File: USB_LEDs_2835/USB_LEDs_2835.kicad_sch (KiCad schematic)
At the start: 53 parts, among them U1 MT9284, U2 JL8022W-L, U3 74LVC1G04

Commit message: Add files via upload
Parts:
- added JP1: solderjumper_1, Jumper:SolderJumper-3_P1.3mm_Bridged12_Pad1.0x1.5mm_NumberLabels, symbol Jumper:SolderJumper_3_Bridged12
- added JP2: solderjumper_2, Jumper:SolderJumper-3_P1.3mm_Bridged12_Pad1.0x1.5mm_NumberLabels, symbol Jumper:SolderJumper_3_Bridged12
- Cx1: value 1u -> 22u; footprint Capacitor_SMD:C_0402_1005Metric -> Capacitor_SMD:C_0603_1608Metric
- D1, D10, D11, D12, D13, D14, D15, D16, D17, D18, D19, D2, D20, D21, D22, D23, D24, D25, D26, D27, D28, D29, D3, D30, D31, D32, D4, D5, D6, D7, D8, D9: footprint LED_SMD:LED_2835 -> LED_SMD:LED_2835_custom_margin
- R1: footprint Resistor_SMD:R_0402_1005Metric -> Resistor_SMD:R_0603_1608Metric
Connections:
- net +5V: now also JP1.1 (A), JP2.3 (B); no longer U2.6 (OPT1)
- net GND: now also JP1.3 (B), JP2.1 (A); no longer U2.8 (OPT2)
- new net: JP1.2 (C), U2.6 (OPT1)
- new net: JP2.2 (C), U2.8 (OPT2)
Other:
- moved on the sheet: C2, H1, H2

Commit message: Add files via upload
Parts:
- D33: footprint Diode_SMD:D_SOD-323 -> Diode_SMD:D_SOD-323_custom
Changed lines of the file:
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@@
       (effects (font (size 1.27 1.27)) (justify left))
     )
-    (property "Footprint" "Diode_SMD:D_SOD-323" (id 2) (at 98.298 78.105 0)
+    (property "Footprint" "Diode_SMD:D_SOD-323_custom" (id 2) (at 98.298 78.105 0)
       (effects (font (size 1.27 1.27)) hide)
     )
@@
     )
     (path "/a4553eb6-c1f2-4b4d-a632-f4d917a8f586"
-      (reference "D33") (unit 1) (value "1N4148WS") (footprint "Diode_SMD:D_SOD-323")
+      (reference "D33") (unit 1) (value "1N4148WS") (footprint "Diode_SMD:D_SOD-323_custom")
     )
     (path "/076783c6-7e48-4539-88e9-ef3e20bf1349"

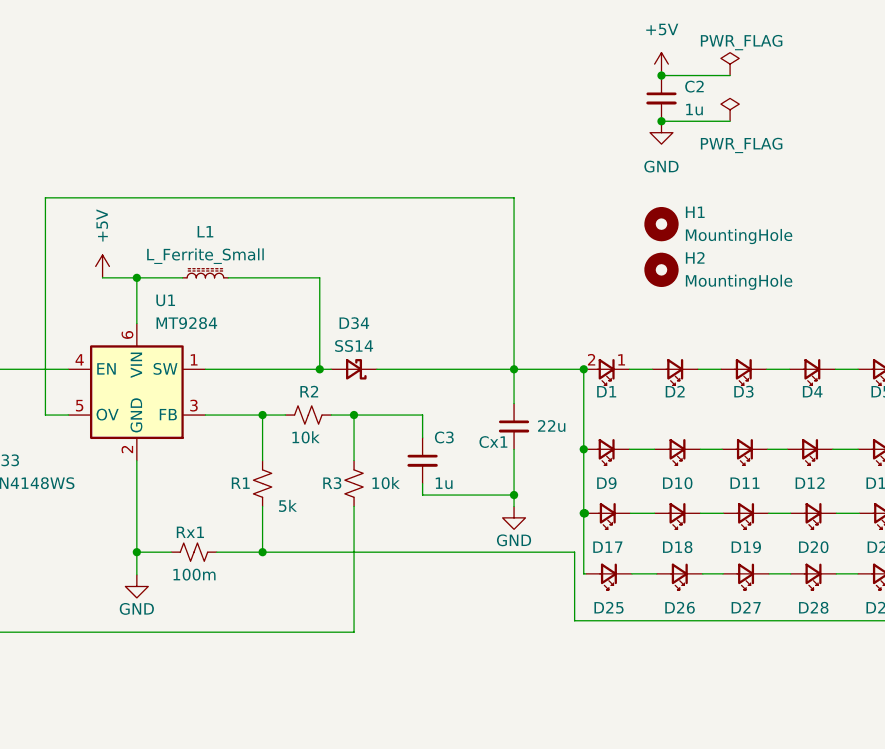
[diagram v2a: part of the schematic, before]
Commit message: Relocated components and compacting the area used
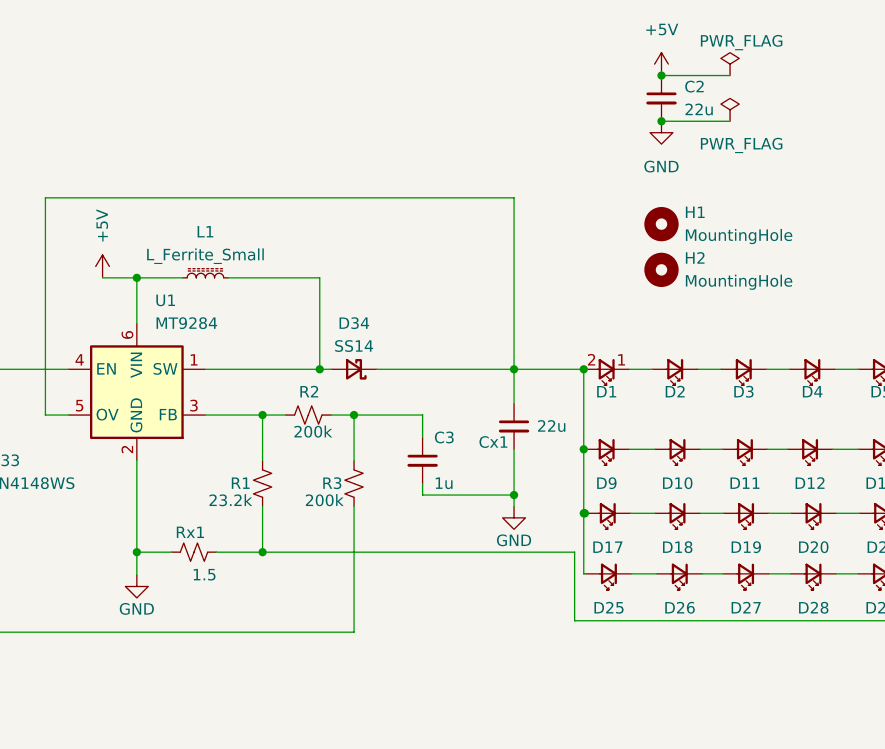
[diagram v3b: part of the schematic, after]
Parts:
- C2: value 1u -> 22u
- R1: value 5k -> 23.2k
- R2, R3: value 10k -> 200k
- Rx1: value 100m -> 1.5
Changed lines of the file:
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@@
       (effects (font (size 1.27 1.27)) (justify left))
     )
-    (property "Value" "1u" (id 1) (at 182.626 37.8522 0)
+    (property "Value" "22u" (id 1) (at 182.626 37.8522 0)
       (effects (font (size 1.27 1.27)) (justify left))
     )
@@
       (effects (font (size 1.27 1.27)) (justify left))
     )
-    (property "Value" "10k" (id 1) (at 151.003 79.375 0)
+    (property "Value" "200k" (id 1) (at 144.78 81.28 0)
       (effects (font (size 1.27 1.27)) (justify left))
     )
@@
       (effects (font (size 1.27 1.27)) (justify left))
     )
-    (property "Value" "5k" (id 1) (at 139.573 81.915 0)
+    (property "Value" "23.2k" (id 1) (at 134.62 81.28 0)
       (effects (font (size 1.27 1.27)) (justify left))
     )
@@
       (effects (font (size 1.27 1.27)) (justify left))
     )
-    (property "Value" "10k" (id 1) (at 142.113 74.295 90)
+    (property "Value" "200k" (id 1) (at 143.51 73.66 90)
       (effects (font (size 1.27 1.27)) (justify left))
     )
@@
       (effects (font (size 1.27 1.27)) (justify left))
     )
-    (property "Value" "100m" (id 1) (at 130.683 89.535 90)
+    (property "Value" "1.5" (id 1) (at 130.683 89.535 90)
       (effects (font (size 1.27 1.27)) (justify left))
     )
@@
     )
     (path "/026f09c8-400d-46f9-844e-0be8161f9746"
-      (reference "C2") (unit 1) (value "1u") (footprint "Capacitor_SMD:C_0402_1005Metric")
+      (reference "C2") (unit 1) (value "22u") (footprint "Capacitor_SMD:C_0402_1005Metric")
     )
     (path "/bc5de113-9719-4067-b963-db31416212e7"
@@
     )
     (path "/46b40edc-42cc-446d-adb2-e52631d88862"
-      (reference "R1") (unit 1) (value "5k") (footprint "Resistor_SMD:R_0603_1608Metric")
+      (reference "R1") (unit 1) (value "23.2k") (footprint "Resistor_SMD:R_0603_1608Metric")
     )
     (path "/66fae963-db90-4b44-b511-1ffbefe55119"
-      (reference "R2") (unit 1) (value "10k") (footprint "Resistor_SMD:R_0402_1005Metric")
+      (reference "R2") (unit 1) (value "200k") (footprint "Resistor_SMD:R_0402_1005Metric")
     )
     (path "/2b40a6ef-b747-4e09-b1c9-aaa6bec91ed5"
-      (reference "R3") (unit 1) (value "10k") (footprint "Resistor_SMD:R_0402_1005Metric")
+      (reference "R3") (unit 1) (value "200k") (footprint "Resistor_SMD:R_0402_1005Metric")
     )
     (path "/b29813e7-e4cd-496d-bb16-c537eb2ab1d5"
@@
     )
     (path "/98753c78-a4c2-4a80-8ed5-3f6f93aecf71"
-      (reference "Rx1") (unit 1) (value "100m") (footprint "Resistor_SMD:R_1206_3216Metric")
+      (reference "Rx1") (unit 1) (value "1.5") (footprint "Resistor_SMD:R_1206_3216Metric")
     )
     (path "/437f8d09-8f17-4205-b86b-2fcaa45bda5d"
